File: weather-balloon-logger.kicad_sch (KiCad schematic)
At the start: 0 parts

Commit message: copperhead: create pipeline stage: schematic
Created the stage-4 deterministic schematic from schematic.intent.json with all 15 fixed-BOM parts, six SUBSYSTEMS groups, 11 functional nets, and six intentional no-connects. Assigned A1/PB08 to one-way OpenLog UART_TX and A0 to default-off cutdown; UART_TX also sinks the 3V3-fed write LED to fit the confirmed two-GPIO budget. Added the complete PINOUT, synchronized BOM/SPEC/SUBSYSTEMS/changelog/decisions/constraints, resolved all affected-item revisits, and verified clean ERC and drift with zero legibility errors.

Verification: ERC clean
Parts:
- added A1: OpenLog, Connector_PinSocket_2.54mm:PinSocket_1x06_P2.54mm_Vertical, symbol Connector_Generic:Conn_01x06
- added C1: 4.7uF, Capacitor_SMD:C_0603_1608Metric, symbol Device:C
- added C2: 100nF, Capacitor_SMD:C_0603_1608Metric, symbol Device:C
- added D1: LTST-C190KGKT, LED_SMD:LED_0603_1608Metric, symbol Device:LED
- added J1, J5: Conn_01x02, Connector_Molex:Molex_Micro-Fit_3.0_43650-0200_1x02_P3.00mm_Horizontal, symbol Connector_Generic:Conn_01x02
- added J2: Conn_01x07, Connector_PinHeader_2.54mm:PinHeader_1x07_P2.54mm_Vertical, symbol Connector_Generic:Conn_01x07
- added J3, J4: SMA, Connector_Coaxial:SMA_Amphenol_132289, symbol Connector:Conn_Coaxial
- added J6: Conn_01x02, Connector_PinHeader_2.54mm:PinHeader_1x02_P2.54mm_Vertical, symbol Connector_Generic:Conn_01x02
- added Q1: AO3400A, Package_TO_SOT_SMD:SOT-23, symbol Transistor_FET:AO3400A
- added R1: 1k, Resistor_SMD:R_0603_1608Metric, symbol Device:R
- added R2: 100R, Resistor_SMD:R_0603_1608Metric, symbol Device:R
- added R3: 1M, Resistor_SMD:R_0603_1608Metric, symbol Device:R
- added SW1: SPDT, Button_Switch_THT:SW_CK_7101MD9CQE, symbol Switch:SW_SPDT
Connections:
- new net 3V3: A1.3 (Pin_3), C1.1, C2.1, J2.3 (Pin_3), R1.1
- new net CUTDOWN_CTRL: J2.7 (Pin_7), R2.1
- new net CUTDOWN_DRAIN: J5.2 (Pin_2), Q1.3 (D)
- new net CUTDOWN_GATE: Q1.1 (G), R2.2, R3.1
- new net GND: A1.2 (Pin_2), C1.2, C2.2, J1.2 (Pin_2), J2.2 (Pin_2), J3.2 (Ext), J4.2 (Ext), Q1.2 (S), R3.2
- new net LED_A: D1.2 (A), R1.2
- new net PACK_IN: J1.1 (Pin_1), SW1.2 (B)
- new net PACK_SW: J2.1 (Pin_1), J5.1 (Pin_1), SW1.1 (A)
- new net RF_APRS: J3.1 (In), J6.1 (Pin_1)
- new net RF_WSPR: J4.1 (In), J6.2 (Pin_2)
- new net UART_TX: A1.5 (Pin_5), D1.1 (K), J2.4 (Pin_4)
- no-connect marks 0 -> 6
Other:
- note added: "1. Power"
- note added: "2. Host / MCU"
- note added: "3.1 UART SD logger"
- note added: "3.2 Antennas"
- note added: "4. UI (operator)"
- note added: "5. Cutdown"
- title: (none) -> weather-balloon-logger

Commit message: copperhead: Revise the host interface and add an I2C LED expander to match the verified LightAPRS-W 2.0 module (docs/SUBSYSTEMS.md section 6). Final pin plan: A1/PB08 = OpenLog UART TX one-way (host TX to OpenLog RXI, no host RX); A2/PB09 = cutdown gate on a direct GPIO (keep R2 series gate resistor and R3 gate pulldown for default-off at power-up); write LED and future GPS-status LEDs on a PCF8574 I2C GPIO expander. (1) Change J2 to the module's 11-position 2.54mm edge header using an installed 11-pin connector symbol Connector_Generic:Conn_01x11, pin order RAW, GND, A1(PB08), A2(PB09), 3V3, GND, SCL, SDA, SCK, MISO, MOSI; wire PACK_SW switched pack+ to RAW, board 3V3 rail from 3V3, GND to the GND pins, A1 to OpenLog RXI, A2 to the cutdown gate network. (2) Add a PCF8574 I2C GPIO expander using an installed KiCad symbol powered from 3V3/GND with a 100nF decoupling cap, address pins strapped for 0x20, SDA/SCL on the module's exposed I2C bus; drive write LED D1 active-low from output P0 (expander output to D1 cathode, D1 anode to 3V3 via R1); leave P1..P7 available for future GPS-satellite-status LEDs as no-connect. (3) Move the cutdown gate source from A0 to A2/PB09, keeping the intentional pulldown so it is default-off. (4) Represent RF as two single contacts HF and VHF at the module opposite bottom corners: VHF to J3 (RF_APRS), HF to J4 (RF_WSPR); replace the 2-pin J6 with the two corner contacts. (5) Update docs/PINOUT.md, docs/BOM.md, docs/SUBSYSTEMS.md and the schematic; keep 3.3V logic and all leakage/idle budgets. Run ERC.
Revised the LightAPRS-W interface to the verified 11-pin J2 order; assigned A1/PB08 to one-way OpenLog UART TX and A2/PB09 to direct default-off cutdown; added PCF8574T U1 at 0x20 with C3, active-low P0 write LED, and P1-P7/INT intentional no-connects; split RF into separate J6 VHF and J7 HF corner contacts; synchronized BOM, pinout, specification, subsystem, bring-up, constraints, decisions, changelog, and firmware pin contracts. ERC, DRC,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
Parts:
- added C3: 100nF, Capacitor_SMD:C_0603_1608Metric, symbol Device:C
- added J7: HF, Connector_PinHeader_2.54mm:PinHeader_1x01_P2.54mm_Vertical, symbol Connector_Generic:Conn_01x01
- added U1: PCF8574T, Package_SO:SOIC-16_3.9x9.9mm_P1.27mm, symbol Interface_Expansion:PCF8574T
- J2: value Conn_01x07 -> Conn_01x11; footprint Connector_PinHeader_2.54mm:PinHeader_1x07_P2.54mm_Vertical -> Connector_PinHeader_2.54mm:PinHeader_1x11_P2.54mm_Vertical; symbol Connector_Generic:Conn_01x07 -> Connector_Generic:Conn_01x11
- J6: value Conn_01x02 -> VHF; footprint Connector_PinHeader_2.54mm:PinHeader_1x02_P2.54mm_Vertical -> Connector_PinHeader_2.54mm:PinHeader_1x01_P2.54mm_Vertical; symbol Connector_Generic:Conn_01x02 -> Connector_Generic:Conn_01x01
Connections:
- net 3V3: now also J2.5 (Pin_5), C3.1, U1.16 (VDD); no longer J2.3 (Pin_3)
- net CUTDOWN_CTRL: now also J2.4 (Pin_4); no longer J2.7 (Pin_7)
- net GND: now also J2.6 (Pin_6), C3.2, U1.1 (A0), U1.2 (A1), U1.3 (A2), U1.8 (GND)
- net RF_WSPR: now also J7.1 (Pin_1); no longer J6.2 (Pin_2)
- net UART_TX: now also J2.3 (Pin_3); no longer D1.1 (K), J2.4 (Pin_4)
- new net I2C_SCL: J2.7 (Pin_7), U1.14 (SCL)
- new net I2C_SDA: J2.8 (Pin_8), U1.15 (SDA)
- new net LED_N: D1.1 (K), U1.4 (P0)
- no-connect marks 6 -> 15
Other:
- moved on the sheet: A1, C1, C2, D1, J1, J3, J4, J5, Q1, R1, R2, R3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

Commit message: feat(pcb): add verified footprint targets
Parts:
- A1: footprint Connector_PinSocket_2.54mm:PinSocket_1x06_P2.54mm_Vertical -> WeatherBalloon:SparkFun_OpenLog_DEV-13712_Carrier
- J1: footprint Connector_Molex:Molex_Micro-Fit_3.0_43650-0200_1x02_P3.00mm_Horizontal -> Connector_JST:JST_PH_S2B-PH-K_1x02_P2.00mm_Horizontal
- J3, J4: footprint Connector_Coaxial:SMA_Amphenol_132289 -> Connector_Coaxial:SMA_Amphenol_132134_Vertical
- J5: footprint Connector_Molex:Molex_Micro-Fit_3.0_43650-0200_1x02_P3.00mm_Horizontal -> Connector_JST:JST_XH_S2B-XH-A_1x02_P2.50mm_Horizontal
- SW1: footprint Button_Switch_THT:SW_CK_7101MD9CQE -> WeatherBalloon:SW_CK_7101SYZQE
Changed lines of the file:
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@@
 			(effects (font (size 1.27 1.27)))
 		)
-		(property "Footprint" "Connector_PinSocket_2.54mm:PinSocket_1x06_P2.54mm_Vertical" (at 144.78 123.19 0)
+		(property "Footprint" "WeatherBalloon:SparkFun_OpenLog_DEV-13712_Carrier" (at 144.78 123.19 0)
 			(effects (font (size 1.27 1.27)) hide)
 		)
@@
 			(effects (font (size 1.27 1.27)))
 		)
-		(property "Footprint" "Connector_Molex:Molex_Micro-Fit_3.0_43650-0200_1x02_P3.00mm_Horizontal" (at 38.1 119.38 0)
+		(property "Footprint" "Connector_JST:JST_PH_S2B-PH-K_1x02_P2.00mm_Horizontal" (at 38.1 119.38 0)
 			(effects (font (size 1.27 1.27)) hide)
 		)
@@
 			(effects (font (size 1.27 1.27)))
 		)
-		(property "Footprint" "Connector_Coaxial:SMA_Amphenol_132289" (at 372.11 119.38 0)
+		(property "Footprint" "Connector_Coaxial:SMA_Amphenol_132134_Vertical" (at 372.11 119.38 0)
 			(effects (font (size 1.27 1.27)) hide)
 		)
@@
 			(effects (font (size 1.27 1.27)))
 		)
-		(property "Footprint" "Connector_Coaxial:SMA_Amphenol_132289" (at 372.11 138.43 0)
+		(property "Footprint" "Connector_Coaxial:SMA_Amphenol_132134_Vertical" (at 372.11 138.43 0)
 			(effects (font (size 1.27 1.27)) hide)
 		)
@@
 			(effects (font (size 1.27 1.27)))
 		)
-		(property "Footprint" "Connector_Molex:Molex_Micro-Fit_3.0_43650-0200_1x02_P3.00mm_Horizontal" (at 273.05 118.11 0)
+		(property "Footprint" "Connector_JST:JST_XH_S2B-XH-A_1x02_P2.50mm_Horizontal" (at 273.05 118.11 0)
 			(effects (font (size 1.27 1.27)) hide)
 		)
@@
 			(effects (font (size 1.27 1.27)))
 		)
-		(property "Footprint" "Button_Switch_THT:SW_CK_7101MD9CQE" (at 64.77 121.92 0)
-			(effects (font (size 1.27 1.27)) hide)
-		)
+		(property "Footprint" "WeatherBalloon:SW_CK_7101SYZQE" (at 64.77 121.92 0)
+			(effects (font (size 1.27 1.27)) hide)
+		)

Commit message: feat(power): capture split logger supply
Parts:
- added A2: Pololu S7V8F5, WeatherBalloon:Pololu_S7V8F5_Carrier, symbol Connector_Generic:Conn_01x04
- added R4: 1k, Resistor_SMD:R_0603_1608Metric, symbol Device:R
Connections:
- net 3V3: no longer A1.3 (Pin_3), C1.1, C2.1
- net GND: now also A2.3 (Pin_3)
- net PACK_SW: now also A2.1 (Pin_1), A2.2 (Pin_2)
- net UART_TX: now also R4.1; no longer A1.5 (Pin_5)
- new net LOGGER_5V: A1.3 (Pin_3), A2.4 (Pin_4), C1.1, C2.1
- new net OPENLOG_RXI: A1.5 (Pin_5), R4.2
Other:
- moved on the sheet: A1, C1, C2, C3, D1, J1, J2, J3, J4, J5, J6, J7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

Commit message: fix(pcb): make R4 through-hole
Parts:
- R4: footprint Resistor_SMD:R_0603_1608Metric -> Resistor_THT:R_Axial_DIN0207_L6.3mm_D2.5mm_P7.62mm_Horizontal
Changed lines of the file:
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@@
 			(effects (font (size 1.27 1.27)))
 		)
-		(property "Footprint" "Resistor_SMD:R_0603_1608Metric" (at 95.25 154.94 0)
+		(property "Footprint" "Resistor_THT:R_Axial_DIN0207_L6.3mm_D2.5mm_P7.62mm_Horizontal" (at 95.25 154.94 0)
 			(effects (font (size 1.27 1.27)) hide)
 		)

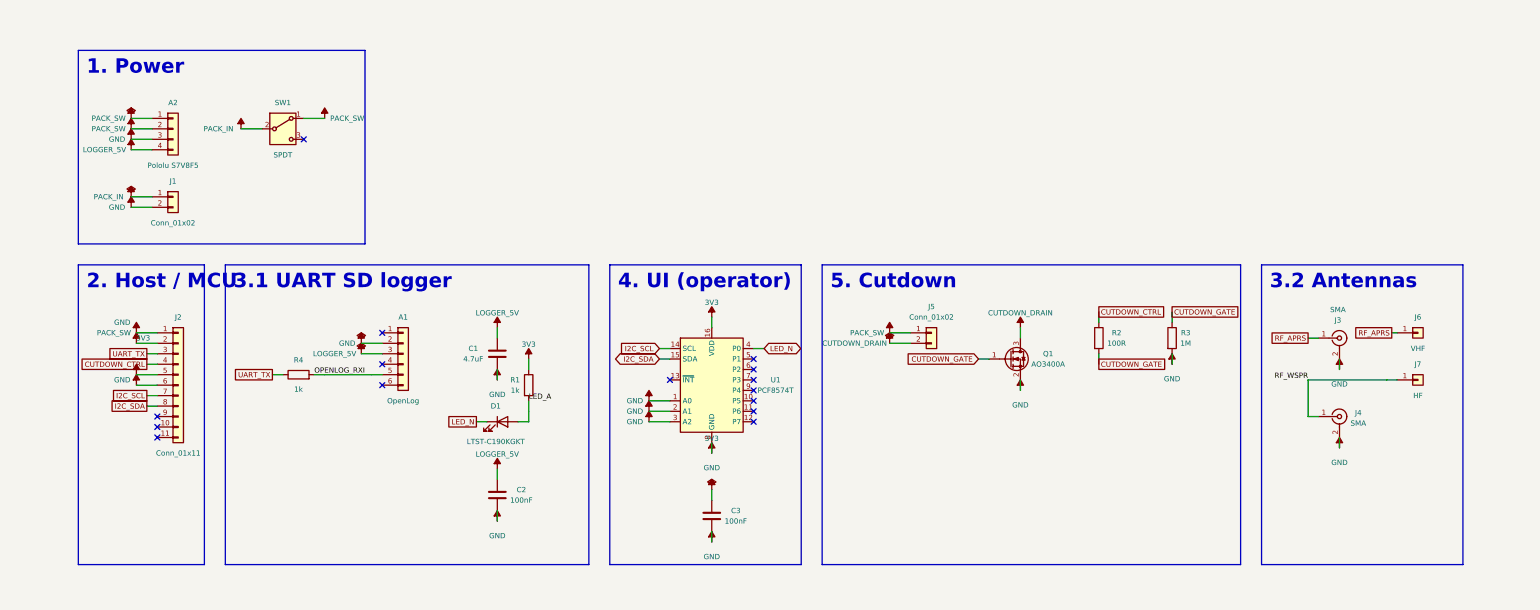
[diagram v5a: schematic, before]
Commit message: copperhead: Final PCB mechanical/legend cleanup. Current electrical DRC is clean with zero unconnected pads. Do not change schematic, intent, BOM, scripts, outline, RF routes, or functional topology. Fix the remaining 30 DRC findings only: move C4 and C5 to eliminate both J5 courtyard overlaps and three PTH-inside-courtyard errors, rerouting only their LOGGER_5V/GND connections while preserving electrical cleanliness; adjust F.SilkS geometry in both project KEMET footprint library files and their embedded C1-C5 board footprints so silk does not cross their own pad solder-mask openings; reposition or hide only reference text and local silk strokes causing the listed U1/R4, J5/C4/C5, U2/R3/Q1, and A2/U2 silk collisions. Preserve fabrication/fab/courtyard dimensions and all pads. Finish with normal KiCad DRC zero violations and zero unconnected items. Do not commit.
Completed the bounded PCB mechanical/legend cleanup without committing. Moved C4 to (107.7,133.3) and C5 to (103,115.5), rerouted only their LOGGER_5V/GND connections, converted both project KEMET footprint silks and all embedded C1-C5 copies to pad-clear strokes, and hid only the identified colliding reference fields. Pads, courtyards, fab geometry, outline, RF routes, schematic, intent, BOM, scripts, and functional topology were preserved. Normal KiCad DRC is clean with zero violations and zero unconnected items; ERC is clean; schematic legibility has no findings; PINOUT drift was reconciled to the unchanged captured cutdown-driver topology.

Verification: ERC clean, DRC clean
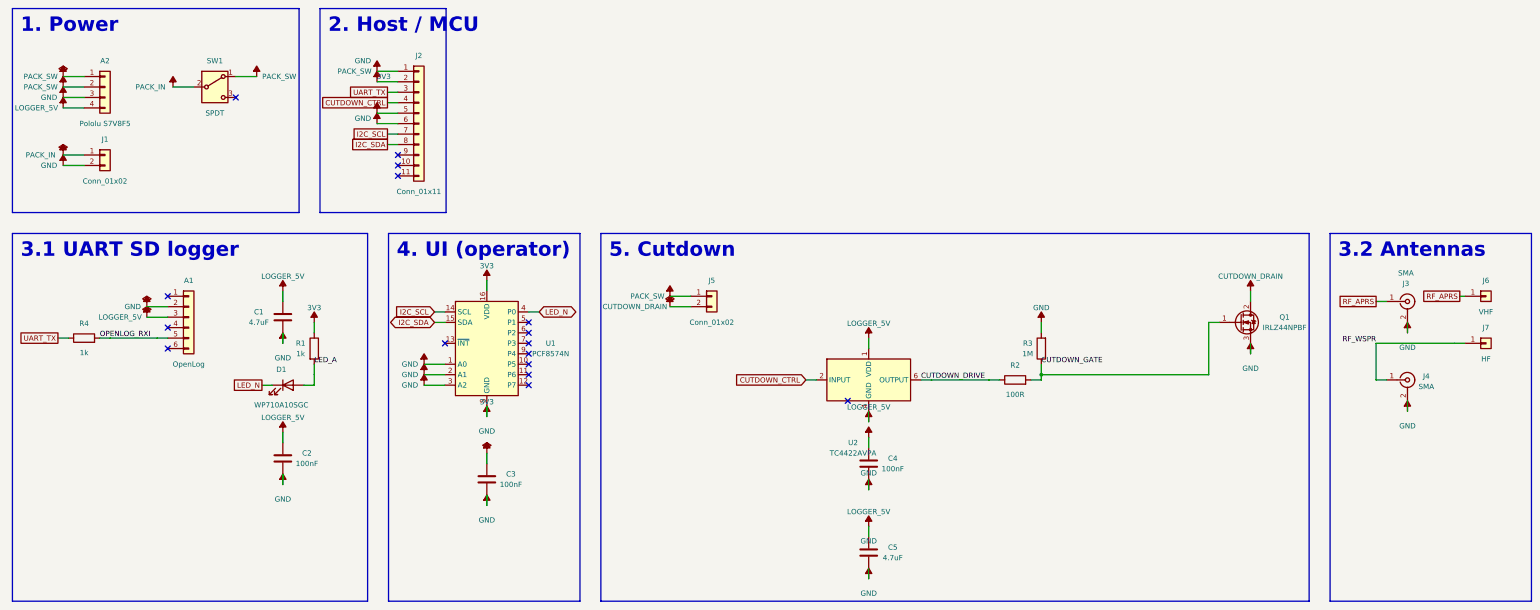
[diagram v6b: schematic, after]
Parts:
- added C4: 100nF, WeatherBalloon:KEMET_C315C104K5R5TA, symbol Device:C
- added C5: 4.7uF, WeatherBalloon:KEMET_C322C475K5R5TA, symbol Device:C
- added U2: TC4422AVPA, Package_DIP:DIP-8_W7.62mm, symbol Driver_FET:TC4422
- C1: footprint Capacitor_SMD:C_0603_1608Metric -> WeatherBalloon:KEMET_C322C475K5R5TA
- C2, C3: footprint Capacitor_SMD:C_0603_1608Metric -> WeatherBalloon:KEMET_C315C104K5R5TA
- D1: value LTST-C190KGKT -> WP710A10SGC; footprint LED_SMD:LED_0603_1608Metric -> LED_THT:LED_D3.0mm
- Q1: value AO3400A -> IRLZ44NPBF; footprint Package_TO_SOT_SMD:SOT-23 -> Package_TO_SOT_THT:TO-220-3_Vertical; symbol Transistor_FET:AO3400A -> Transistor_FET:IRLZ44N
- R1, R2, R3: footprint Resistor_SMD:R_0603_1608Metric -> Resistor_THT:R_Axial_DIN0207_L6.3mm_D2.5mm_P7.62mm_Horizontal
- U1: value PCF8574T -> PCF8574N; footprint Package_SO:SOIC-16_3.9x9.9mm_P1.27mm -> Package_DIP:DIP-16_W7.62mm; symbol Interface_Expansion:PCF8574T -> Interface_Expansion:PCF8574P
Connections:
- net CUTDOWN_CTRL: now also U2.2 (INPUT); no longer R2.1
- net CUTDOWN_DRAIN: now also Q1.2 (D); no longer Q1.3 (D)
- net GND: now also Q1.3 (S), C4.2, C5.2, U2.4 (GND), U2.5 (GND); no longer Q1.2 (S)
- net LOGGER_5V: now also C4.1, C5.1, U2.1 (VDD), U2.8 (VDD)
- new net CUTDOWN_DRIVE: R2.1, U2.6 (OUTPUT), U2.7 (OUTPUT)
- no-connect marks 15 -> 16
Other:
- moved on the sheet: A1, A2, C1, C2, C3, D1, J1, J2, J3, J4, J5, J6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

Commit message: chore(fab): add release readiness checks
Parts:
- A1: MPN (none) -> DEV-13955
- A2: MPN (none) -> Pololu item 2123
- C1, C5: MPN (none) -> C322C475K5R5TA
- C2, C3, C4: MPN (none) -> C315C104K5R5TA
- D1: MPN (none) -> WP710A10SGC
- J1: MPN (none) -> S2B-PH-K-S(LF)(SN)
- J2: MPN (none) -> 61301111121
- J3, J4: MPN (none) -> 132134
- J5: MPN (none) -> S2B-XH-A(LF)(SN)
- J6, J7: MPN (none) -> 61300111121
- Q1: MPN (none) -> IRLZ44NPBF
- R1, R4: MPN (none) -> MFR-25FBF52-1K
- R2: MPN (none) -> MFR-25FBF52-100R
- R3: MPN (none) -> MFR-25FBF52-1M
- SW1: MPN (none) -> 7101SYZQE
- U1: MPN (none) -> PCF8574N
- U2: MPN (none) -> TC4422AVPA
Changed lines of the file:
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@@
+			(effects (font (size 1.27 1.27)) hide)
+		)
+		(property "MPN" "DEV-13955" (at 68.58 140.97 0)
 			(effects (font (size 1.27 1.27)) hide)
 		)
@@
 			(effects (font (size 1.27 1.27)) hide)
 		)
+		(property "MPN" "Pololu item 2123" (at 48.26 85.09 0)
+			(effects (font (size 1.27 1.27)) hide)
+		)
 		(pin "1")
 		(pin "2")
@@
 			(effects (font (size 1.27 1.27)) hide)
 		)
+		(property "MPN" "C322C475K5R5TA" (at 91.44 140.97 0)
+			(effects (font (size 1.27 1.27)) hide)
+		)
 		(pin "1")
 		(pin "2")
@@
 			(effects (font (size 1.27 1.27)) hide)
 		)
+		(property "MPN" "C315C104K5R5TA" (at 91.44 175.26 0)
+			(effects (font (size 1.27 1.27)) hide)
+		)
 		(pin "1")
 		(pin "2")
@@
 			(effects (font (size 1.27 1.27)) hide)
 		)
+		(property "MPN" "C315C104K5R5TA" (at 140.97 180.34 0)
+			(effects (font (size 1.27 1.27)) hide)
+		)
 		(pin "1")
 		(pin "2")
@@
 			(effects (font (size 1.27 1.27)) hide)
 		)
+		(property "MPN" "C315C104K5R5TA" (at 233.68 176.53 0)
+			(effects (font (size 1.27 1.27)) hide)
+		)
 		(pin "1")
 		(pin "2")
@@
 			(effects (font (size 1.27 1.27)) hide)
 		)
+		(property "MPN" "C322C475K5R5TA" (at 233.68 198.12 0)
+			(effects (font (size 1.27 1.27)) hide)
+		)
 		(pin "1")
 		(pin "2")
@@
 			(effects (font (size 1.27 1.27)) hide)
 		)
+		(property "MPN" "WP710A10SGC" (at 92.71 157.48 0)
+			(effects (font (size 1.27 1.27)) hide)
+		)
 		(pin "1")
 		(pin "2")
@@
 			(effects (font (size 1.27 1.27)) hide)
 		)
+		(property "MPN" "S2B-PH-K-S(LF)(SN)" (at 48.26 101.6 0)
+			(effects (font (size 1.27 1.27)) hide)
+		)
 		(pin "1")
 		(pin "2")
@@
 		)
 		(property "Datasheet" "~" (at 124.46 93.98 0)
+			(effects (font (size 1.27 1.27)) hide)
+		)
+		(property "MPN" "61301111121" (at 124.46 93.98 0)
 			(effects (font (size 1.27 1.27)) hide)
 		)
@@
 			(effects (font (size 1.27 1.27)) hide)
 		)
+		(property "MPN" "132134" (at 364.49 137.16 0)
+			(effects (font (size 1.27 1.27)) hide)
+		)
 		(pin "1")
 		(pin "2")
@@
 			(effects (font (size 1.27 1.27)) hide)
 		)
+		(property "MPN" "132134" (at 364.49 156.21 0)
+			(effects (font (size 1.27 1.27)) hide)
+		)
 		(pin "1")
 		(pin "2")
@@
 			(effects (font (size 1.27 1.27)) hide)
 		)
+		(property "MPN" "S2B-XH-A(LF)(SN)" (at 195.58 135.89 0)
+			(effects (font (size 1.27 1.27)) hide)
+		)
 		(pin "1")
 		(pin "2")
@@
 			(effects (font (size 1.27 1.27)) hide)
 		)
+		(property "MPN" "61300111121" (at 383.54 135.89 0)
+			(effects (font (size 1.27 1.27)) hide)
+		)
 		(pin "1")
 		(instances
@@
 			(effects (font (size 1.27 1.27)) hide)
 		)
+		(property "MPN" "61300111121" (at 383.54 147.32 0)
+			(effects (font (size 1.27 1.27)) hide)
+		)
 		(pin "1")
 		(instances
@@
 			(effects (font (size 1.27 1.27)) hide)
 		)
+		(property "MPN" "IRLZ44NPBF" (at 323.85 142.24 0)
+			(effects (font (size 1.27 1.27)) hide)
+		)
 		(pin "1")
 		(pin "2")
@@
 			(effects (font (size 1.27 1.27)) hide)
 		)
+		(property "MPN" "MFR-25FBF52-1K" (at 99.06 148.59 0)
+			(effects (font (size 1.27 1.27)) hide)
+		)
 		(pin "1")
 		(pin "2")
@@
 			(effects (font (size 1.27 1.27)) hide)
 		)
+		(property "MPN" "MFR-25FBF52-100R" (at 269.24 156.21 0)
+			(effects (font (size 1.27 1.27)) hide)
+		)
 		(pin "1")
 		(pin "2")
@@
 			(effects (font (size 1.27 1.27)) hide)
 		)
+		(property "MPN" "MFR-25FBF52-1M" (at 275.59 148.59 0)
+			(effects (font (size 1.27 1.27)) hide)
+		)
 		(pin "1")
 		(pin "2")
@@
 			(effects (font (size 1.27 1.27)) hide)
 		)
+		(property "MPN" "MFR-25FBF52-1K" (at 43.18 146.05 0)
+			(effects (font (size 1.27 1.27)) hide)
+		)
 		(pin "1")
 		(pin "2")
@@
 			(effects (font (size 1.27 1.27)) hide)
 		)
+		(property "MPN" "7101SYZQE" (at 74.93 85.09 0)
+			(effects (font (size 1.27 1.27)) hide)
+		)
 		(pin "1")
 		(pin "2")
@@
 		)
 		(property "Datasheet" "~" (at 140.97 149.86 0)
+			(effects (font (size 1.27 1.27)) hide)
+		)
+		(property "MPN" "PCF8574N" (at 140.97 149.86 0)
 			(effects (font (size 1.27 1.27)) hide)
 		)
@@
 			(effects (font (size 1.27 1.27)) hide)
 		)
+		(property "MPN" "TC4422AVPA" (at 233.68 156.21 0)
+			(effects (font (size 1.27 1.27)) hide)
+		)
